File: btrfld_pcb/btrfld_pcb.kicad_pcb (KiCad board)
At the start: 2 copper layers, 82 x 64.8 mm, 39 parts

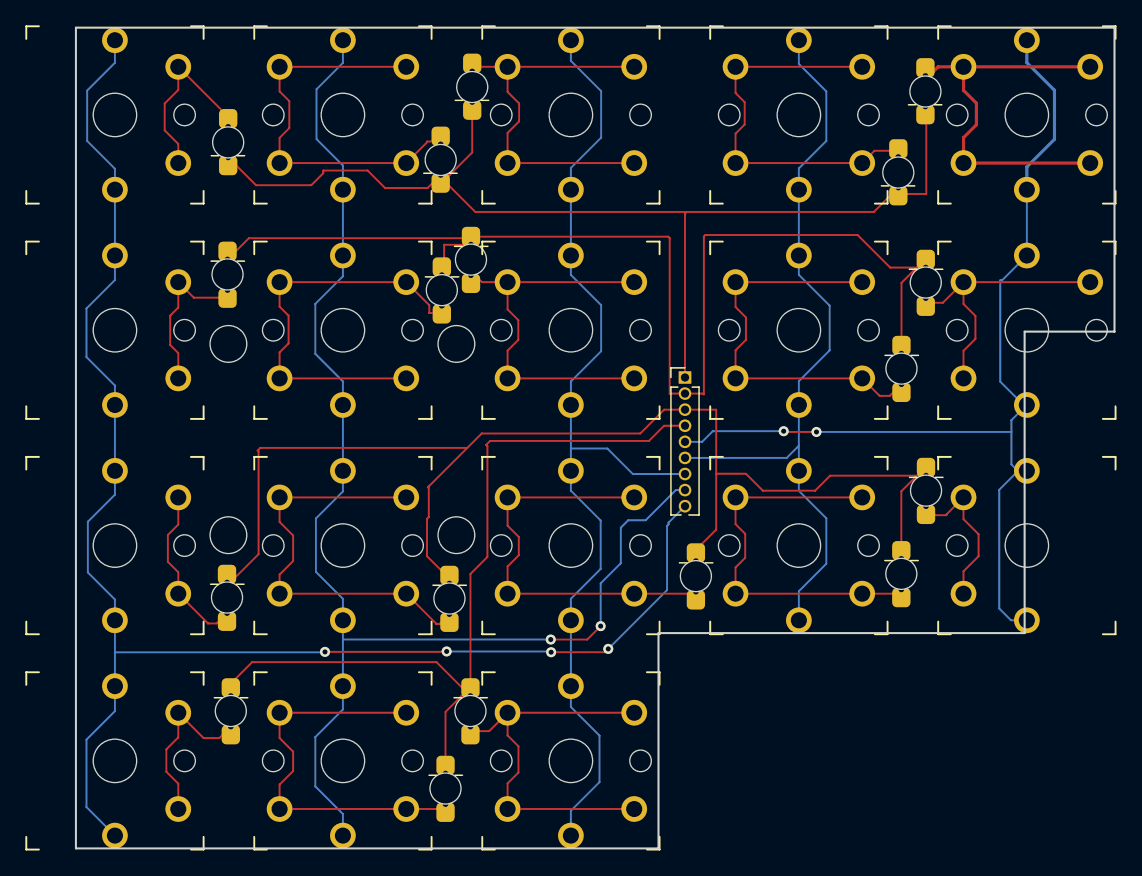
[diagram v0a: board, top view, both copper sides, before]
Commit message: fixup flipped diode holes so copper connects pads on either side of board
also fixup some tracing while we are at it
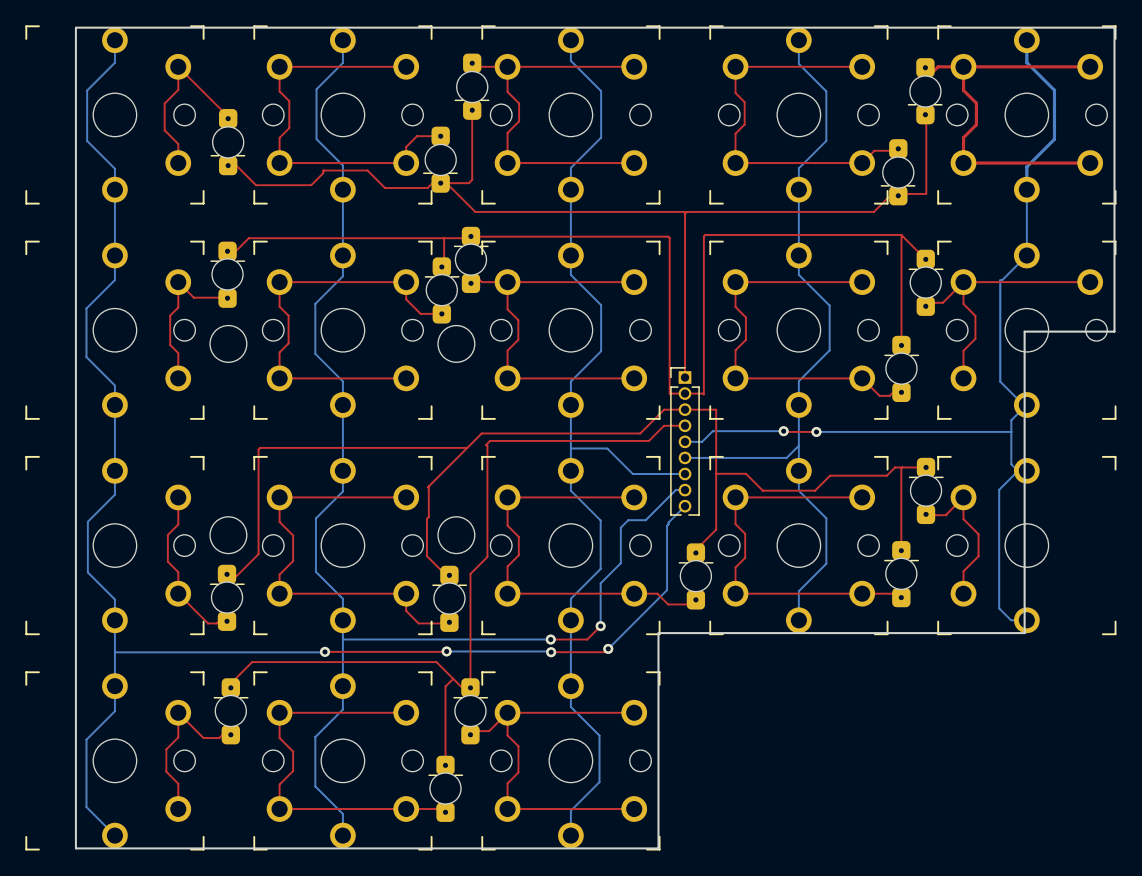
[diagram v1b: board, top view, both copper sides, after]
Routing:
- net (no net): track 1272.7 -> 1277.4 mm
